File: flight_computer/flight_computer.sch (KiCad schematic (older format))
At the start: 0 parts

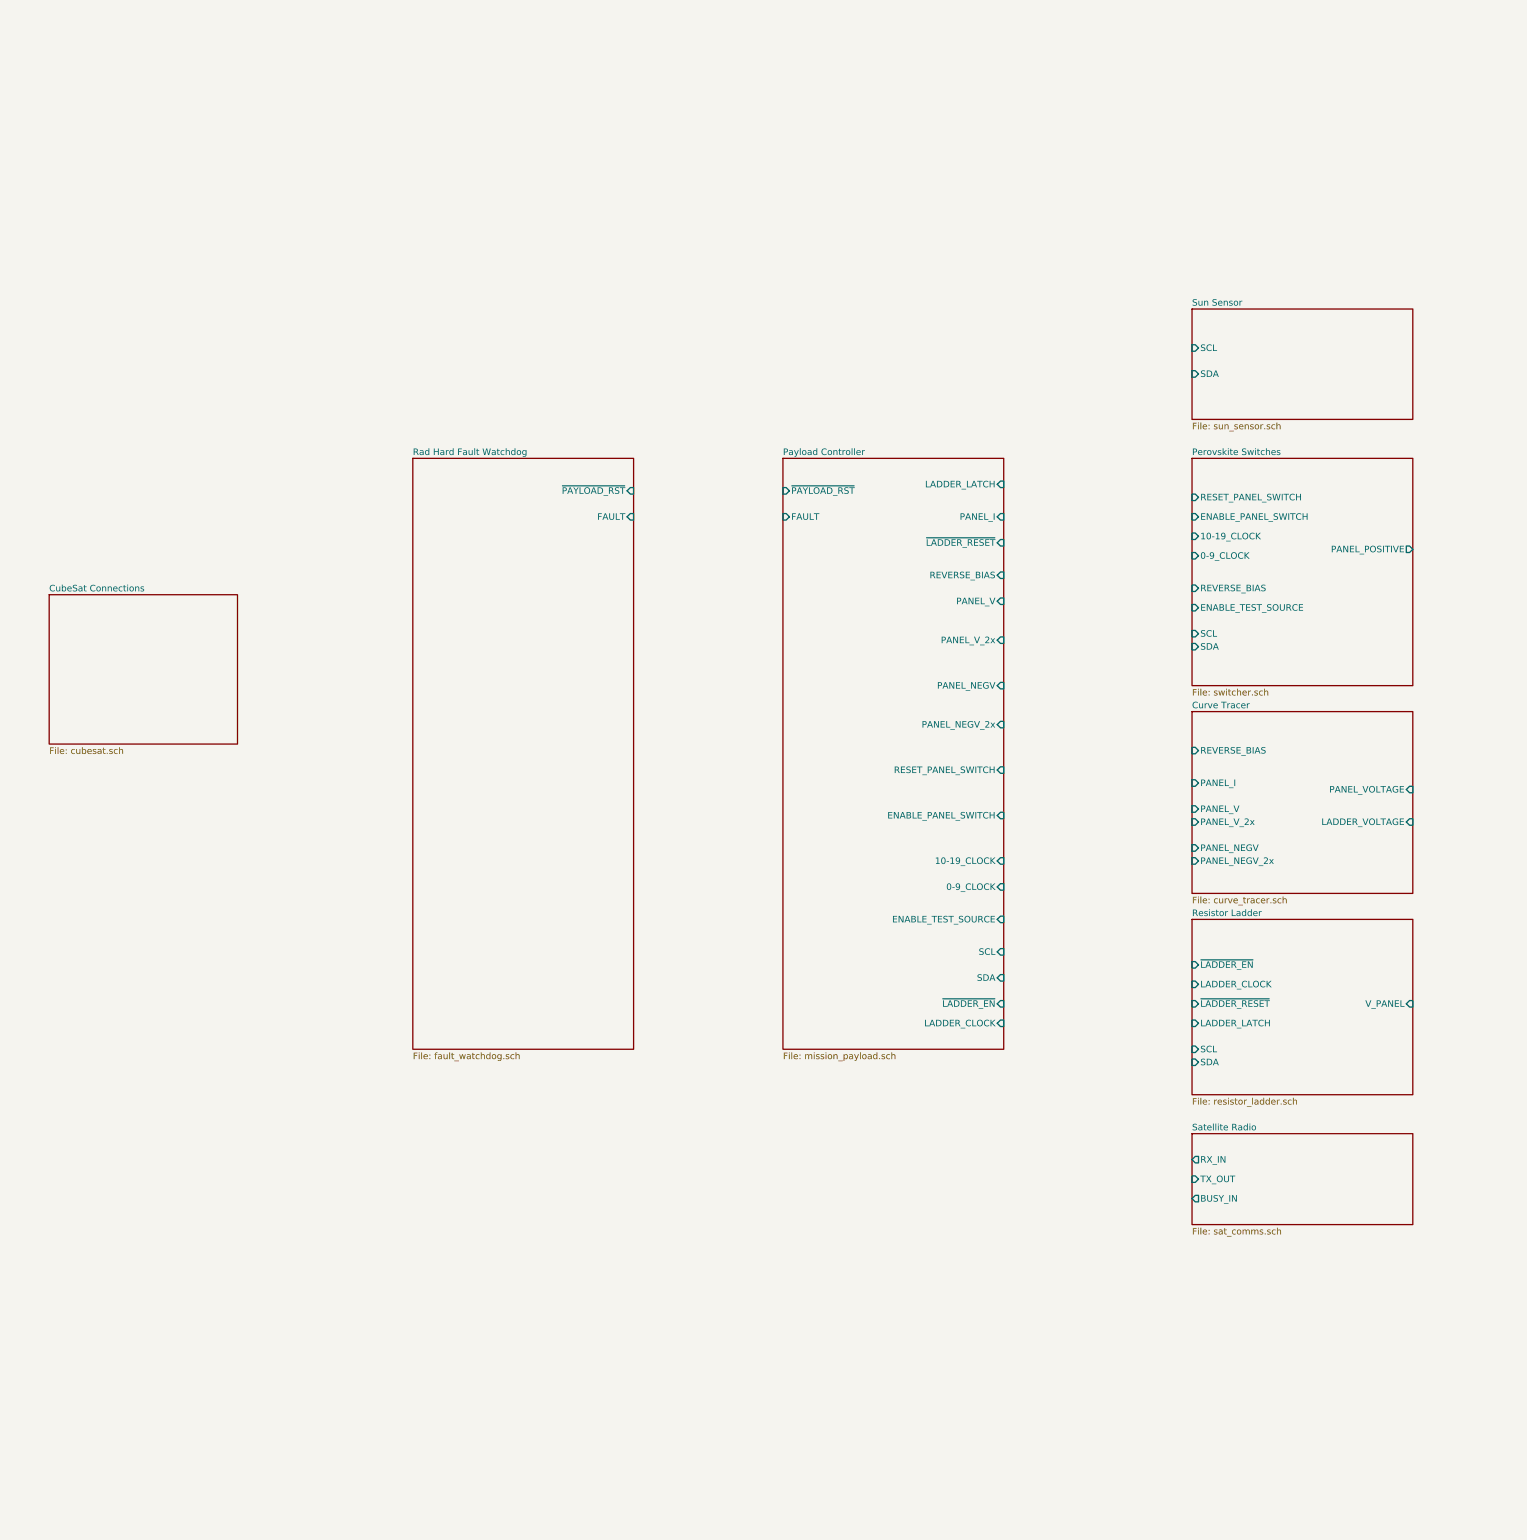
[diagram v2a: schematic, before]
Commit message: Update flight computer schematic
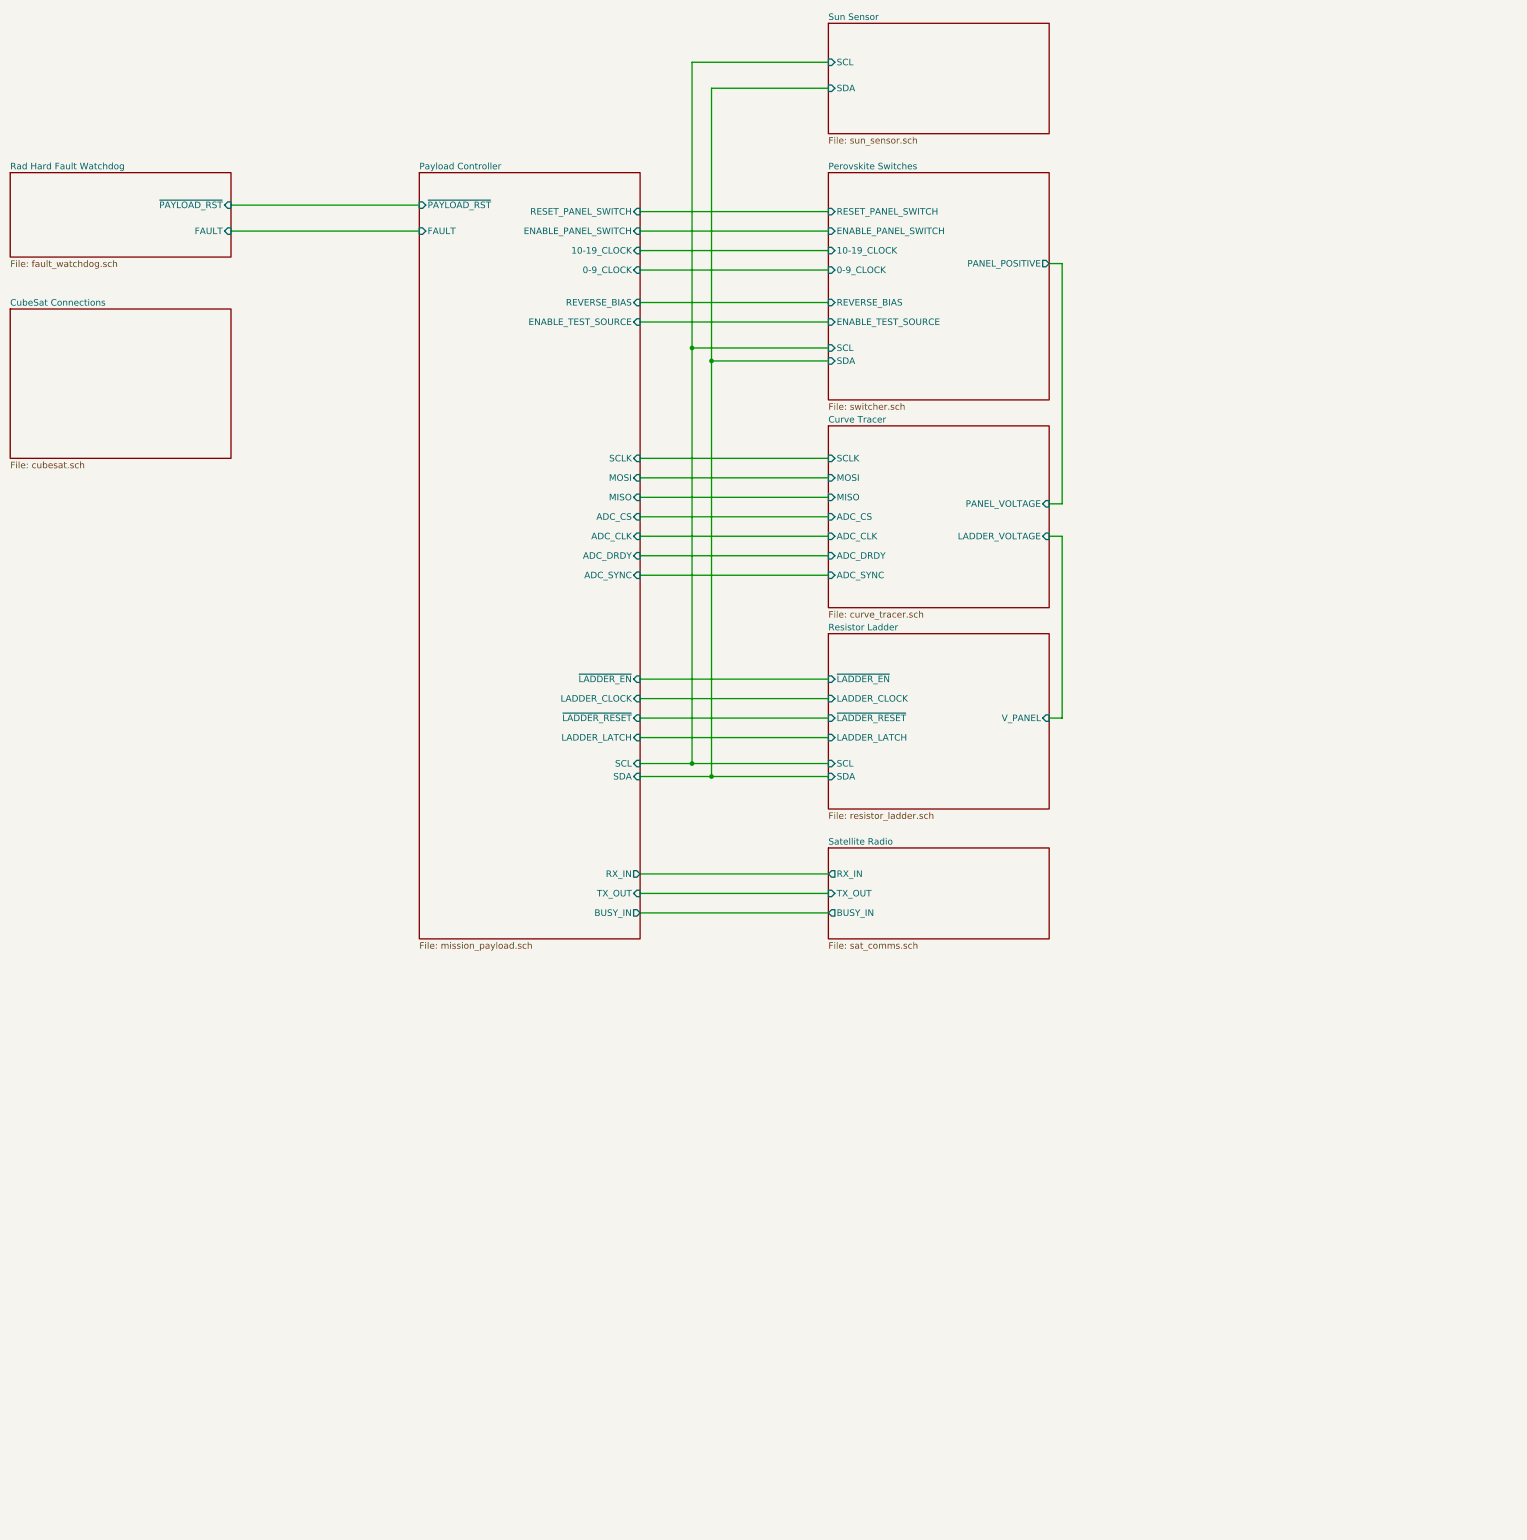
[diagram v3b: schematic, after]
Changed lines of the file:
@@
 EELAYER 30 0
 EELAYER END
-$Descr A2 23386 16535
+$Descr A3 16535 11693
 encoding utf-8
 Sheet 1 9
@@
 $EndDescr
 $Sheet
-S 13750 8700 1700 1350
+S 10950 6500 1700 1350
 U 635FEB2F
 F0 "Resistor Ladder" 50
 F1 "resistor_ladder.sch" 50
-F2 "V_PANEL" I R 15450 9350 50
-F3 "~LADDER_EN" I L 13750 9050 50
-F4 "LADDER_CLOCK" I L 13750 9200 50
-F5 "~LADDER_RESET" I L 13750 9350 50
-F6 "LADDER_LATCH" I L 13750 9500 50
-F7 "SCL" I L 13750 9700 50
-F8 "SDA" I L 13750 9800 50
-$EndSheet
-$Sheet
-S 13750 7100 1700 1400
+F2 "V_PANEL" I R 12650 7150 50
+F3 "~LADDER_EN" I L 10950 6850 50
+F4 "LADDER_CLOCK" I L 10950 7000 50
+F5 "~LADDER_RESET" I L 10950 7150 50
+F6 "LADDER_LATCH" I L 10950 7300 50
+F7 "SCL" I L 10950 7500 50
+F8 "SDA" I L 10950 7600 50
+$EndSheet
+$Sheet
+S 10950 4900 1700 1400
 U 63C503EE
 F0 "Curve Tracer" 50
 F1 "curve_tracer.sch" 50
-F2 "PANEL_VOLTAGE" I R 15450 7700 50
-F3 "LADDER_VOLTAGE" I R 15450 7950 50
-F4 "PANEL_V" I L 13750 7850 50
-F5 "PANEL_I" I L 13750 7650 50
-F6 "PANEL_V_2x" I L 13750 7950 50
-F7 "REVERSE_BIAS" I L 13750 7400 50
-F8 "PANEL_NEGV" I L 13750 8150 50
-F9 "PANEL_NEGV_2x" I L 13750 8250 50
-$EndSheet
-$Sheet
-S 13750 5150 1700 1750
+F2 "PANEL_VOLTAGE" I R 12650 5500 50
+F3 "LADDER_VOLTAGE" I R 12650 5750 50
+F4 "SCLK" I L 10950 5150 50
+F5 "MOSI" I L 10950 5300 50
+F6 "MISO" I L 10950 5450 50
+F7 "ADC_CS" I L 10950 5600 50
+F8 "ADC_CLK" I L 10950 5750 50
+F9 "ADC_DRDY" I L 10950 5900 50
+F10 "ADC_SYNC" I L 10950 6050 50
+$EndSheet
+$Sheet
+S 10950 2950 1700 1750
 U 635FE71D
 F0 "Perovskite Switches" 50
 F1 "switcher.sch" 50
-F2 "ENABLE_TEST_SOURCE" I L 13750 6300 50
-F3 "RESET_PANEL_SWITCH" I L 13750 5450 50
-F4 "ENABLE_PANEL_SWITCH" I L 13750 5600 50
-F5 "10-19_CLOCK" I L 13750 5750 50
-F6 "0-9_CLOCK" I L 13750 5900 50
-F7 "PANEL_POSITIVE" O R 15450 5850 50
-F8 "REVERSE_BIAS" I L 13750 6150 50
-F9 "SDA" I L 13750 6600 50
-F10 "SCL" I L 13750 6500 50
-$EndSheet
-$Sheet
-S 7750 5150 1700 4550
+F2 "ENABLE_TEST_SOURCE" I L 10950 4100 50
+F3 "RESET_PANEL_SWITCH" I L 10950 3250 50
+F4 "ENABLE_PANEL_SWITCH" I L 10950 3400 50
+F5 "10-19_CLOCK" I L 10950 3550 50
+F6 "0-9_CLOCK" I L 10950 3700 50
+F7 "PANEL_POSITIVE" O R 12650 3650 50
+F8 "REVERSE_BIAS" I L 10950 3950 50
+F9 "SDA" I L 10950 4400 50
+F10 "SCL" I L 10950 4300 50
+$EndSheet
+$Sheet
+S 4650 2950 1700 650
 U 63D1F518
 F0 "Rad Hard Fault Watchdog" 50
 F1 "fault_watchdog.sch" 50
-F2 "FAULT" I R 9450 5600 50
-F3 "~PAYLOAD_RST" I R 9450 5400 50
-$EndSheet
-$Sheet
-S 10600 5150 1700 4550
+F2 "FAULT" I R 6350 3400 50
+F3 "~PAYLOAD_RST" I R 6350 3200 50
+$EndSheet
+$Sheet
+S 7800 2950 1700 5900
 U 63D21EEE
 F0 "Payload Controller" 50
 F1 "mission_payload.sch" 50
-F2 "PANEL_I" I R 12300 5600 50
-F3 "REVERSE_BIAS" I R 12300 6050 50
-F4 "PANEL_V" I R 12300 6250 50
-F5 "PANEL_V_2x" I R 12300 6550 50
-F6 "PANEL_NEGV" I R 12300 6900 50
-F7 "PANEL_NEGV_2x" I R 12300 7200 50
-F8 "RESET_PANEL_SWITCH" I R 12300 7550 50
-F9 "ENABLE_PANEL_SWITCH" I R 12300 7900 50
-F10 "10-19_CLOCK" I R 12300 8250 50
-F11 "0-9_CLOCK" I R 12300 8450 50
-F12 "ENABLE_TEST_SOURCE" I R 12300 8700 50
-F13 "SCL" I R 12300 8950 50
-F14 "SDA" I R 12300 9150 50
-F15 "~LADDER_EN" I R 12300 9350 50
-F16 "LADDER_CLOCK" I R 12300 9500 50
-F17 "~LADDER_RESET" I R 12300 5800 50
-F18 "LADDER_LATCH" I R 12300 5350 50
-F19 "~PAYLOAD_RST" I L 10600 5400 50
-F20 "FAULT" I L 10600 5600 50
-$EndSheet
-$Sheet
-S 4950 6200 1450 1150
+F2 "~PAYLOAD_RST" I L 7800 3200 50
+F3 "FAULT" I L 7800 3400 50
+F4 "RESET_PANEL_SWITCH" I R 9500 3250 50
+F5 "ENABLE_PANEL_SWITCH" I R 9500 3400 50
+F6 "10-19_CLOCK" I R 9500 3550 50
+F7 "0-9_CLOCK" I R 9500 3700 50
+F8 "ENABLE_TEST_SOURCE" I R 9500 4100 50
+F9 "SCL" I R 9500 7500 50
+F10 "SDA" I R 9500 7600 50
+F11 "~LADDER_EN" I R 9500 6850 50
+F12 "LADDER_CLOCK" I R 9500 7000 50
+F13 "~LADDER_RESET" I R 9500 7150 50
+F14 "LADDER_LATCH" I R 9500 7300 50
+F15 "SCLK" I R 9500 5150 50
+F16 "MOSI" I R 9500 5300 50
+F17 "MISO" I R 9500 5450 50
+F18 "ADC_CLK" I R 9500 5750 50
+F19 "ADC_CS" I R 9500 5600 50
+F20 "ADC_DRDY" I R 9500 5900 50
+F21 "ADC_SYNC" I R 9500 6050 50
+F22 "RX_IN" O R 9500 8350 50
+F23 "TX_OUT" I R 9500 8500 50
+F24 "BUSY_IN" O R 9500 8650 50
+F25 "REVERSE_BIAS" I R 9500 3950 50
+$EndSheet
+$Sheet
+S 4650 4000 1700 1150
 U 63D2A1A8
 F0 "CubeSat Connections" 50
@@
 $EndSheet
 $Sheet
-S 13750 4000 1700 850
+S 10950 1800 1700 850
 U 63D2A1C8
 F0 "Sun Sensor" 50
 F1 "sun_sensor.sch" 50
-F2 "SCL" I L 13750 4300 50
-F3 "SDA" I L 13750 4500 50
-$EndSheet
-$Sheet
-S 13750 10350 1700 700
+F2 "SCL" I L 10950 2100 50
+F3 "SDA" I L 10950 2300 50
+$EndSheet
+$Sheet
+S 10950 8150 1700 700
 U 63D2A1FC
 F0 "Satellite Radio" 50
 F1 "sat_comms.sch" 50
-F2 "RX_IN" O L 13750 10550 50
-F3 "TX_OUT" I L 13750 10700 50
-F4 "BUSY_IN" O L 13750 10850 50
-$EndSheet
+F2 "RX_IN" O L 10950 8350 50
+F3 "TX_OUT" I L 10950 8500 50
+F4 "BUSY_IN" O L 10950 8650 50
+$EndSheet
+Wire Wire Line
+	9500 7500 9900 7500
+Wire Wire Line
+	10950 7600 10050 7600
+Wire Wire Line
+	10950 2100 9900 2100
+Wire Wire Line
+	9900 2100 9900 4300
+Connection ~ 9900 7500
+Wire Wire Line
+	9900 7500 10950 7500
+Wire Wire Line
+	10950 2300 10050 2300
+Wire Wire Line
+	10050 2300 10050 4400
+Connection ~ 10050 7600
+Wire Wire Line
+	10050 7600 9500 7600
+Wire Wire Line
+	10950 4300 9900 4300
+Connection ~ 9900 4300
+Wire Wire Line
+	9900 4300 9900 7500
+Wire Wire Line
+	10950 4400 10050 4400
+Connection ~ 10050 4400
+Wire Wire Line
+	10050 4400 10050 7600
+Wire Wire Line
+	9500 3250 10950 3250
+Wire Wire Line
+	9500 3400 10950 3400
+Wire Wire Line
+	9500 3550 10950 3550
+Wire Wire Line
+	9500 3700 10950 3700
+Wire Wire Line
+	9500 3950 10950 3950
+Wire Wire Line
+	9500 4100 10950 4100
+Wire Wire Line
+	9500 5150 10950 5150
+Wire Wire Line
+	9500 5300 10950 5300
+Wire Wire Line
+	9500 5450 10950 5450
+Wire Wire Line
+	9500 5600 10950 5600
+Wire Wire Line
+	9500 5750 10950 5750
+Wire Wire Line
+	9500 5900 10950 5900
+Wire Wire Line
+	9500 6050 10950 6050
+Wire Wire Line
+	9500 6850 10950 6850
+Wire Wire Line
+	9500 7000 10950 7000
+Wire Wire Line
+	9500 7150 10950 7150
+Wire Wire Line
+	9500 7300 10950 7300
+Wire Wire Line
+	9500 8350 10950 8350
+Wire Wire Line
+	9500 8500 10950 8500
+Wire Wire Line
+	9500 8650 10950 8650
+Wire Wire Line
+	6350 3200 7800 3200
+Wire Wire Line
+	6350 3400 7800 3400
+Wire Wire Line
+	12650 3650 12750 3650
+Wire Wire Line
+	12750 3650 12750 5500
+Wire Wire Line
+	12750 5500 12650 5500
+Wire Wire Line
+	12650 5750 12750 5750
+Wire Wire Line
+	12750 5750 12750 7150
+Wire Wire Line
+	12750 7150 12650 7150
 $EndSCHEMATC
